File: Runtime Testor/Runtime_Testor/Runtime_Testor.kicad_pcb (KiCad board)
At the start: 2 copper layers, 56.9 x 24.4 mm, 37 parts, among them CON1 SWD, J1 ESP8266, J2 USB_A, SW1 SW_SPDT, SW2 SW_Push, U1 FRAM, U2 AMS1117-3.3, U3 STM32F103C8T6, Y1 16MHz

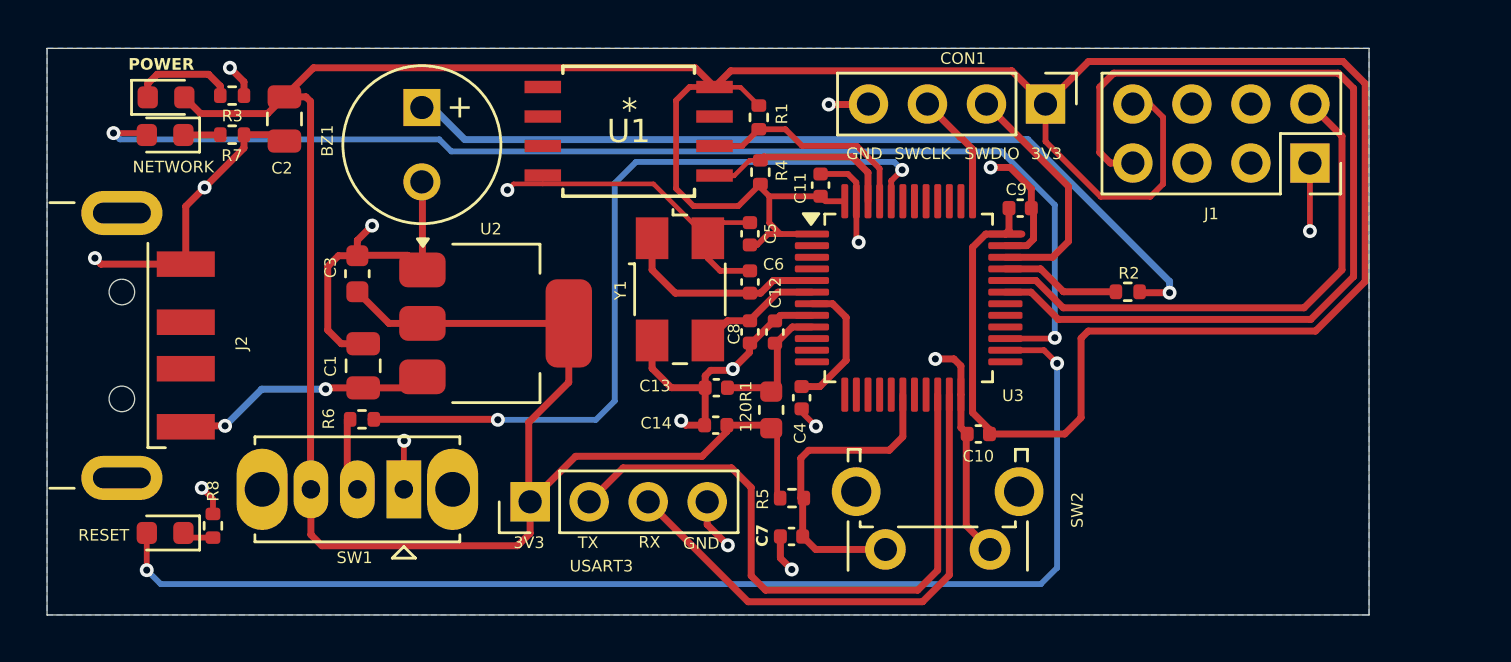
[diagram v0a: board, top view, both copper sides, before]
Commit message: Added USB Port for UART communication
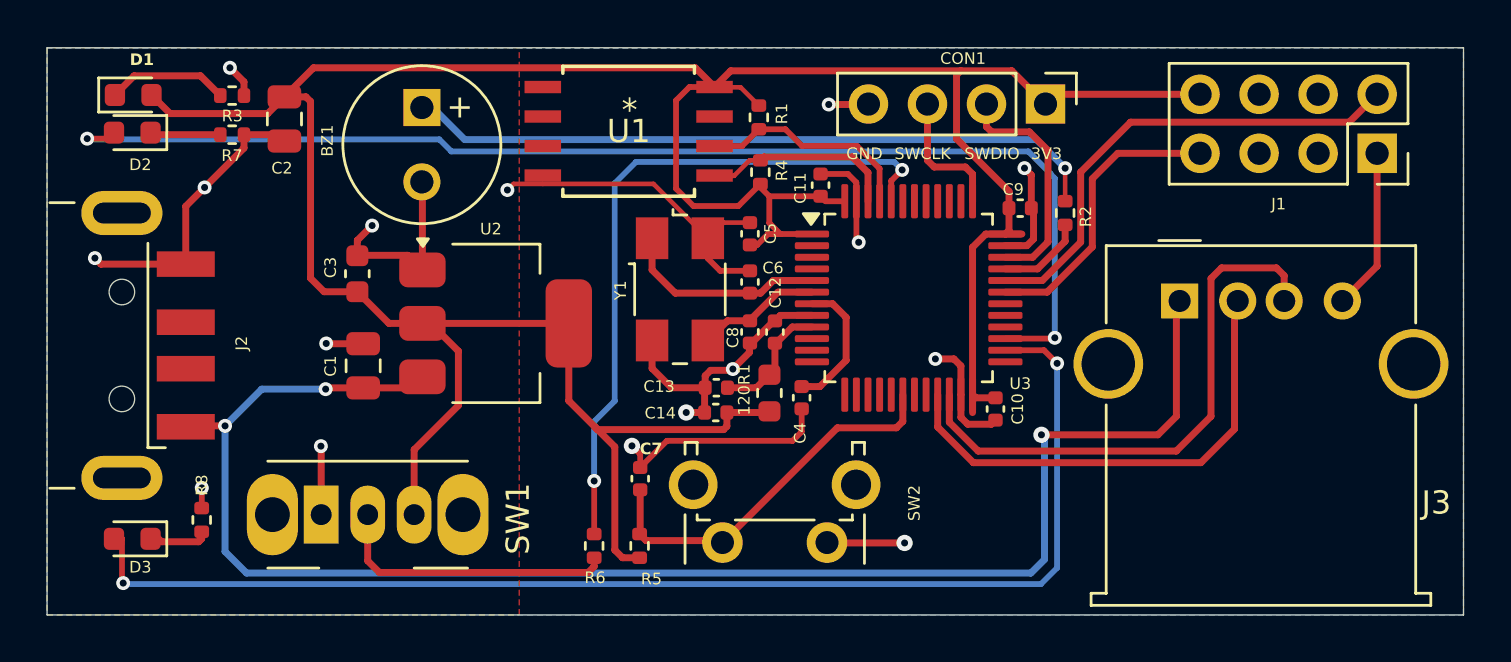
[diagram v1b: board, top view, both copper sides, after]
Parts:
- removed USART3: CON, Connector_PinHeader_2.54mm:PinHeader_1x04_P2.54mm_Vertical
- added J3: USB_A, Connector_USB:USB_A_Molex_67643_Horizontal, F.Cu at (191.0, 75.9)
- SW1: footprint Button_Switch_THT:SW_Slide_SPDT_Straight_CK_OS102011MS2Q -> Button_Switch_THT:SW_Slide_SPDT_Angled_CK_OS102011MA1Q
- moved R6 11.4 mm to (165.8, 86.4), turned to 90 degrees
- moved SW2 7.02 mm to (175.8, 86.3)
- moved C7 6.97 mm to (167.8, 83.5), turned to 90 degrees
- moved R5 6.87 mm to (167.7, 86.4), turned to 90 degrees
- moved R2 4.33 mm to (186.1, 72.1), turned to 90 degrees
- moved SW1 3.72 mm to (154.0, 85.1), turned to 0 degrees
- moved J1 2.92 mm to (199.5, 69.5)
- moved D3 1.43 mm to (145.9, 86.1)
- moved D1 1.42 mm to (145.9, 67.0)
- moved D2 1.42 mm to (145.9, 68.7)
- moved C10 1.31 mm to (183.1, 80.5), turned to -90 degrees
- moved 120R1 0.73 mm to (173.3, 79.9)
- moved R8 0.55 mm to (148.9, 85.3)
- moved C14 0.54 mm to (171.0, 80.7)
- renumbered POWER to D1, NETWORK to D2, RESET to D3
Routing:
- net VBUS: track 11.1 -> 69.0 mm, vias 2 -> 3
- net +3.3V: track 193.6 -> 139.1 mm
- net /ESP_RX: track 40.2 -> 12.6 mm
- net /SW_Boot0: track 3.19 -> 12.4 mm
- net Net-(BZ1-+): track 37.3 -> 30.4 mm
- net /USART3_TX: track 27.9 -> 21.2 mm
- net /BOOT0: track 34.6 -> 29.9 mm
- net Net-(U3-PB0): track 13.8 -> 16.7 mm
- net /ESP_TX: track 23.4 -> 21.1 mm
- net GND: track 89.1 -> 91.0 mm, vias 17 -> 16
- net /NETWORK: track 51.1 -> 52.6 mm
- net Net-(D2-K): track 1.59 -> 3.05 mm
- net /Buzzer: track 5.16 -> 3.77 mm
- net /USART3_RX: track 23.0 -> 24.1 mm
- net /RESET: track 52.6 -> 53.7 mm
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- added copper zone on F.Cu, net GND
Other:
- board size 56.9 x 24.4 mm -> 61 x 24.4 mm
- board text removed: "RX"
- board text removed: "TX"
